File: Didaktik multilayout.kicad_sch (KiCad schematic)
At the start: 103 parts, among them J1 Conn_01x04_MountingPin, J2 AVR-ISP-6, SW1 SW_Push_45deg, SW10 SW_Push_45deg, SW11 SW_Push_45deg, SW12 SW_Push_45deg, SW13 SW_Push_45deg, SW14 SW_Push_45deg, SW15 SW_Push_45deg, SW16 SW_Push_45deg, SW17 SW_Push_45deg, SW18 SW_Push_45deg, SW19 SW_Push_45deg, SW2 SW_Push_45deg, SW20 SW_Push_45deg, SW21 SW_Push_45deg, SW22 SW_Push_45deg, SW23 SW_Push_45deg, SW24 SW_Push_45deg, SW25 SW_Push_45deg, SW26 SW_Push_45deg, SW27 SW_Push_45deg, SW28 SW_Push_45deg, SW29 SW_Push_45deg, SW3 SW_Push_45deg, SW30 SW_Push_45deg, SW31 SW_Push_45deg, SW32 SW_Push_45deg, SW33 SW_Push_45deg, SW34 SW_Push_45deg, SW35 SW_Push_45deg, SW36 SW_Push_45deg, SW37 SW_Push_45deg, SW38 SW_Push_45deg, SW39 SW_Push_45deg, SW4 SW_Push_45deg, SW40 SW_Push_45deg, SW5 SW_Push_45deg, SW6 SW_Push_45deg, SW7 SW_Push_45deg, SW8 SW_Push_45deg, SW9 SW_Push_45deg, U1 ATmega32U4-M, Y1 Crystal_GND24_Small

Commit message: routing multipcb
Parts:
- added SW31a1, SW32a1, SW33a1, SW34a1, SW37a1, SW38a1, SW39a1, SW40a1: SW_Push_45deg, Keebio-Parts:MX-Alps-Choc-1U-NoLED, symbol Switch:SW_Push_45deg
- added SW34b1, SW37b1: SW_Push_45deg, Keebio-Parts:MX-Alps-Choc-3U-NoLED-StabFlip, symbol Switch:SW_Push_45deg
- added SW35a1, SW36a1: SW_Push_45deg, Keebio-Parts:MX-Alps-Choc-1.5U-NoLED, symbol Switch:SW_Push_45deg
- added SW35b1, SW36b1: SW_Push_45deg, Keebio-Parts:MX-Alps-Choc-2U-NoLED-StabFlip, symbol Switch:SW_Push_45deg
- added SW35c1: SW_Push_45deg, Keebio-Parts:MX-Alps-Choc-6U-NoLED-StabFlip, symbol Switch:SW_Push_45deg
- added SW36c1: SW_Push_45deg, Keebio-Parts:MX-Alps-Choc-7U-NoLED-StabFlip, symbol Switch:SW_Push_45deg
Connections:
- net COL0: now also SW31a1.1, SW32a1.1
- net COL1: now also SW33a1.1, SW34a1.1, SW34b1.1
- net COL2: now also SW35a1.1, SW35b1.1, SW35c1.1, SW36a1.1, SW36b1.1, SW36c1.1
- net COL3: now also SW37a1.1, SW37b1.1, SW38a1.1
- net COL4: now also SW39a1.1, SW40a1.1
- net MISO: now also U1.20 (PD2); no longer U1.28 (PB4)
- net MOSI: now also U1.21 (PD3); no longer U1.26 (PD6)
- net ROW4: now also U1.30 (PB6); no longer U1.22 (PD5)
- net ROW5: now also U1.29 (PB5); no longer U1.21 (PD3)
- net ROW6: now also U1.28 (PB4); no longer U1.30 (PB6)
- net ROW7: now also U1.27 (PD7); no longer U1.29 (PB5)
- net SCK: now also U1.22 (PD5); no longer U1.27 (PD7)
- net at D37.2 (A), SW39.2: now also SW39a1.2
- net at D8.2 (A), SW32.2: now also SW32a1.2
- net at D33.2 (A), SW38.2: now also SW38a1.2
- net at D20.2 (A), SW35.2: now also SW35a1.2, SW35b1.2, SW35c1.2, SW36c1.2
- net at D41.2 (A), SW40.2: now also SW40a1.2
- net at D24.2 (A), SW36.2: now also SW36a1.2, SW36b1.2
- net at D12.2 (A), SW33.2: now also SW33a1.2
- net at D16.2 (A), SW34.2: now also SW34a1.2, SW34b1.2
- net at D29.2 (A), SW37.2: now also SW37a1.2, SW37b1.2
- net at D4.2 (A), SW31.2: now also SW31a1.2

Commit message: set up multilayout
need to check if all switches are really routed
maybe get rid of 2U
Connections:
- net MISO: now also U1.21 (PD3); no longer U1.20 (PD2)
- net MOSI: now also U1.22 (PD5); no longer U1.21 (PD3)
- net SCK: now also U1.20 (PD2); no longer U1.22 (PD5)
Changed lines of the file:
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@@
     )
   )
-  (global_label "MOSI" (shape input) (at 85.09 78.74 0) (fields_autoplaced)
+  (global_label "MOSI" (shape input) (at 85.09 83.82 0) (fields_autoplaced)
     (effects (font (size 1.27 1.27)) (justify left))
-    (property "Intersheet References" "${INTERSHEET_REFS}" (id 0) (at 92.0993 78.6606 0)
+    (property "Intersheet References" "${INTERSHEET_REFS}" (id 0) (at 92.0993 83.7406 0)
       (effects (font (size 1.27 1.27)) (justify left) hide)
     )
@@
     )
   )
-  (global_label "MISO" (shape input) (at 85.09 76.2 0) (fields_autoplaced)
+  (global_label "MISO" (shape input) (at 85.09 78.74 0) (fields_autoplaced)
     (effects (font (size 1.27 1.27)) (justify left))
-    (property "Intersheet References" "${INTERSHEET_REFS}" (id 0) (at 92.0993 76.1206 0)
+    (property "Intersheet References" "${INTERSHEET_REFS}" (id 0) (at 92.0993 78.6606 0)
       (effects (font (size 1.27 1.27)) (justify left) hide)
     )
@@
     )
   )
-  (global_label "SCK" (shape input) (at 85.09 83.82 0) (fields_autoplaced)
+  (global_label "SCK" (shape input) (at 85.09 76.2 0) (fields_autoplaced)
     (effects (font (size 1.27 1.27)) (justify left))
-    (property "Intersheet References" "${INTERSHEET_REFS}" (id 0) (at 91.2526 83.7406 0)
+    (property "Intersheet References" "${INTERSHEET_REFS}" (id 0) (at 91.2526 76.1206 0)
       (effects (font (size 1.27 1.27)) (justify left) hide)
     )

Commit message: changes
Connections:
- net GND: now also J1.MP (MountPin)
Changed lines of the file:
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@@
   (junction (at 37.465 146.05) (diameter 0) (color 0 0 0 0)
   )
+  (junction (at 69.215 185.42) (diameter 0) (color 0 0 0 0)
+  )
   (junction (at 189.23 69.85) (diameter 0) (color 0 0 0 0)
   )
@@
     (stroke (width 0) (type default) (color 0 0 0 0))
   )
+  (wire (pts (xy 74.295 190.5) (xy 69.215 190.5))
+    (stroke (width 0) (type default) (color 0 0 0 0))
+  )
   (wire (pts (xy 170.18 83.185) (xy 170.18 102.87))
     (stroke (width 0) (type default) (color 0 0 0 0))
@@
     (stroke (width 0) (type default) (color 0 0 0 0))
   )
+  (wire (pts (xy 69.215 190.5) (xy 69.215 185.42))
+    (stroke (width 0) (type default) (color 0 0 0 0))
+  )

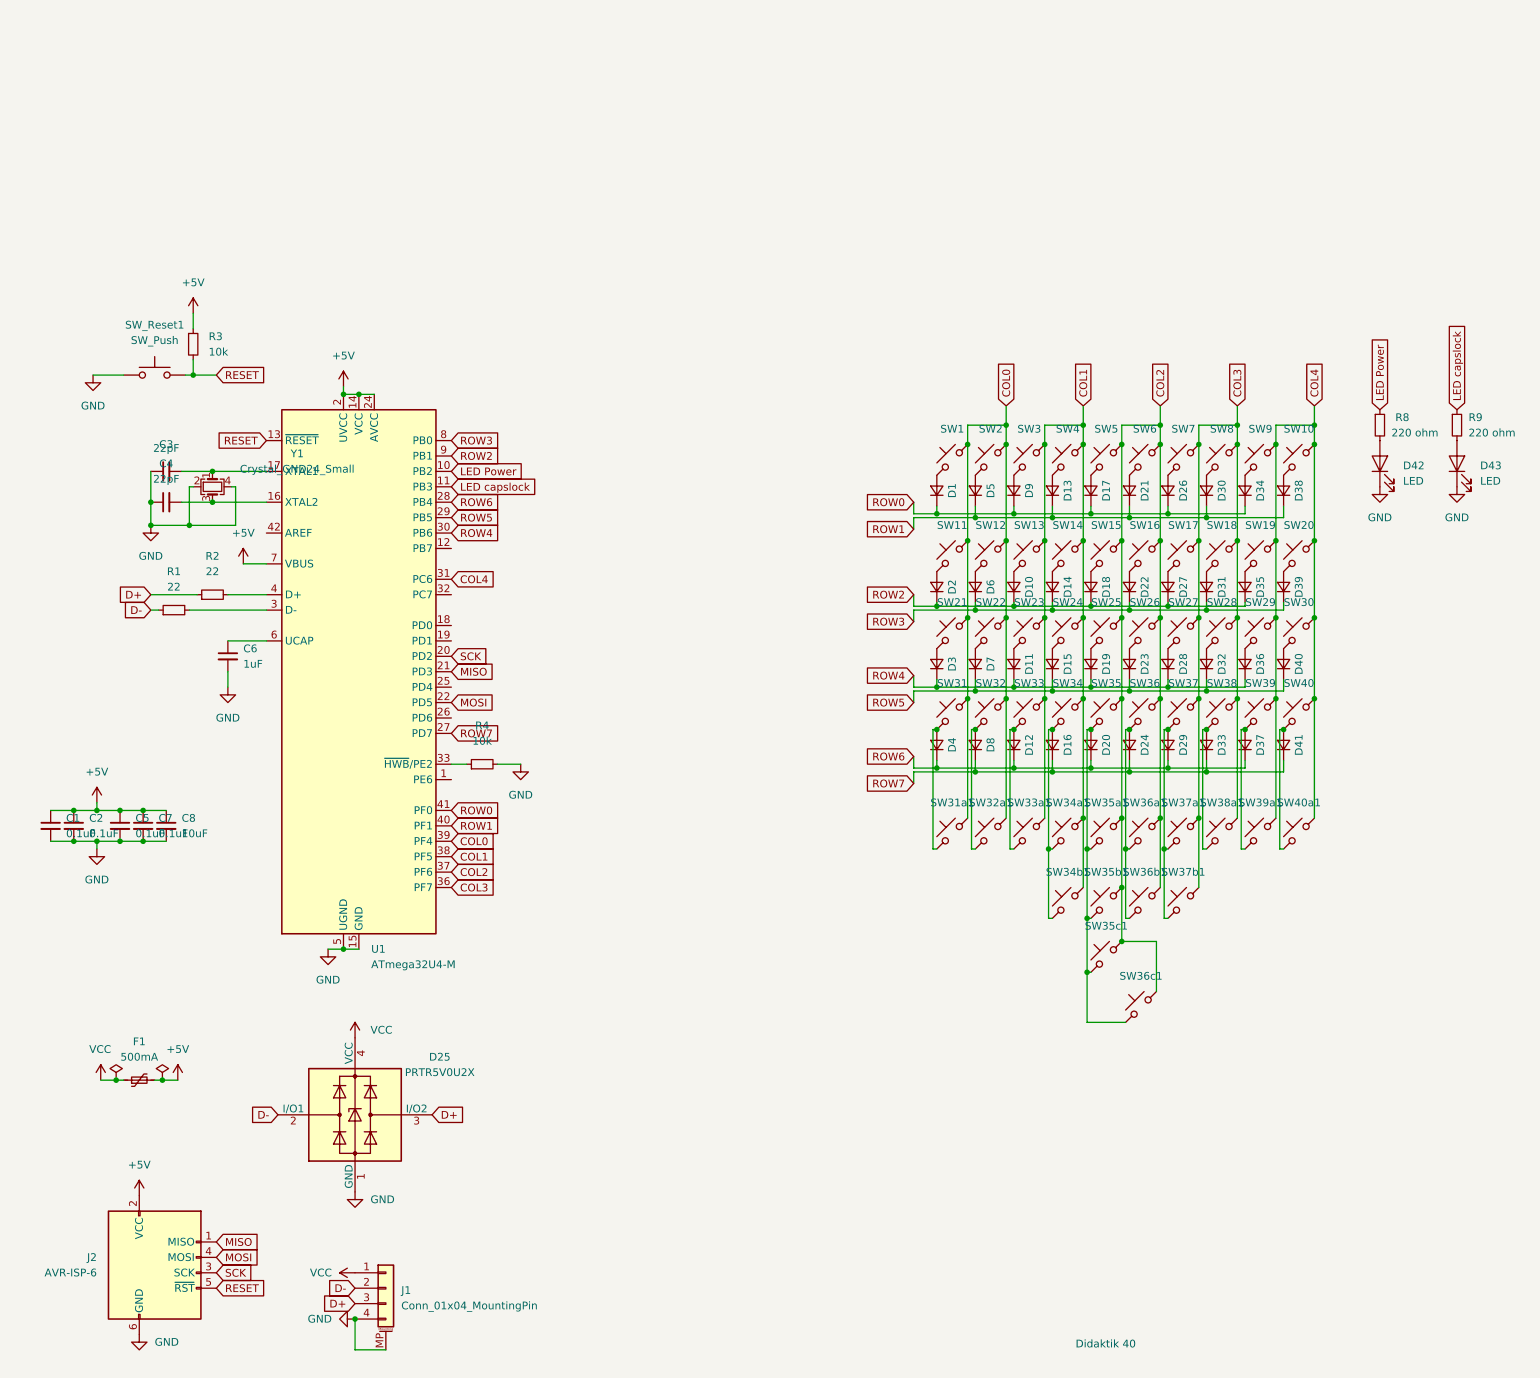
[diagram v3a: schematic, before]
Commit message: simplifying schematics, rerouting pcb
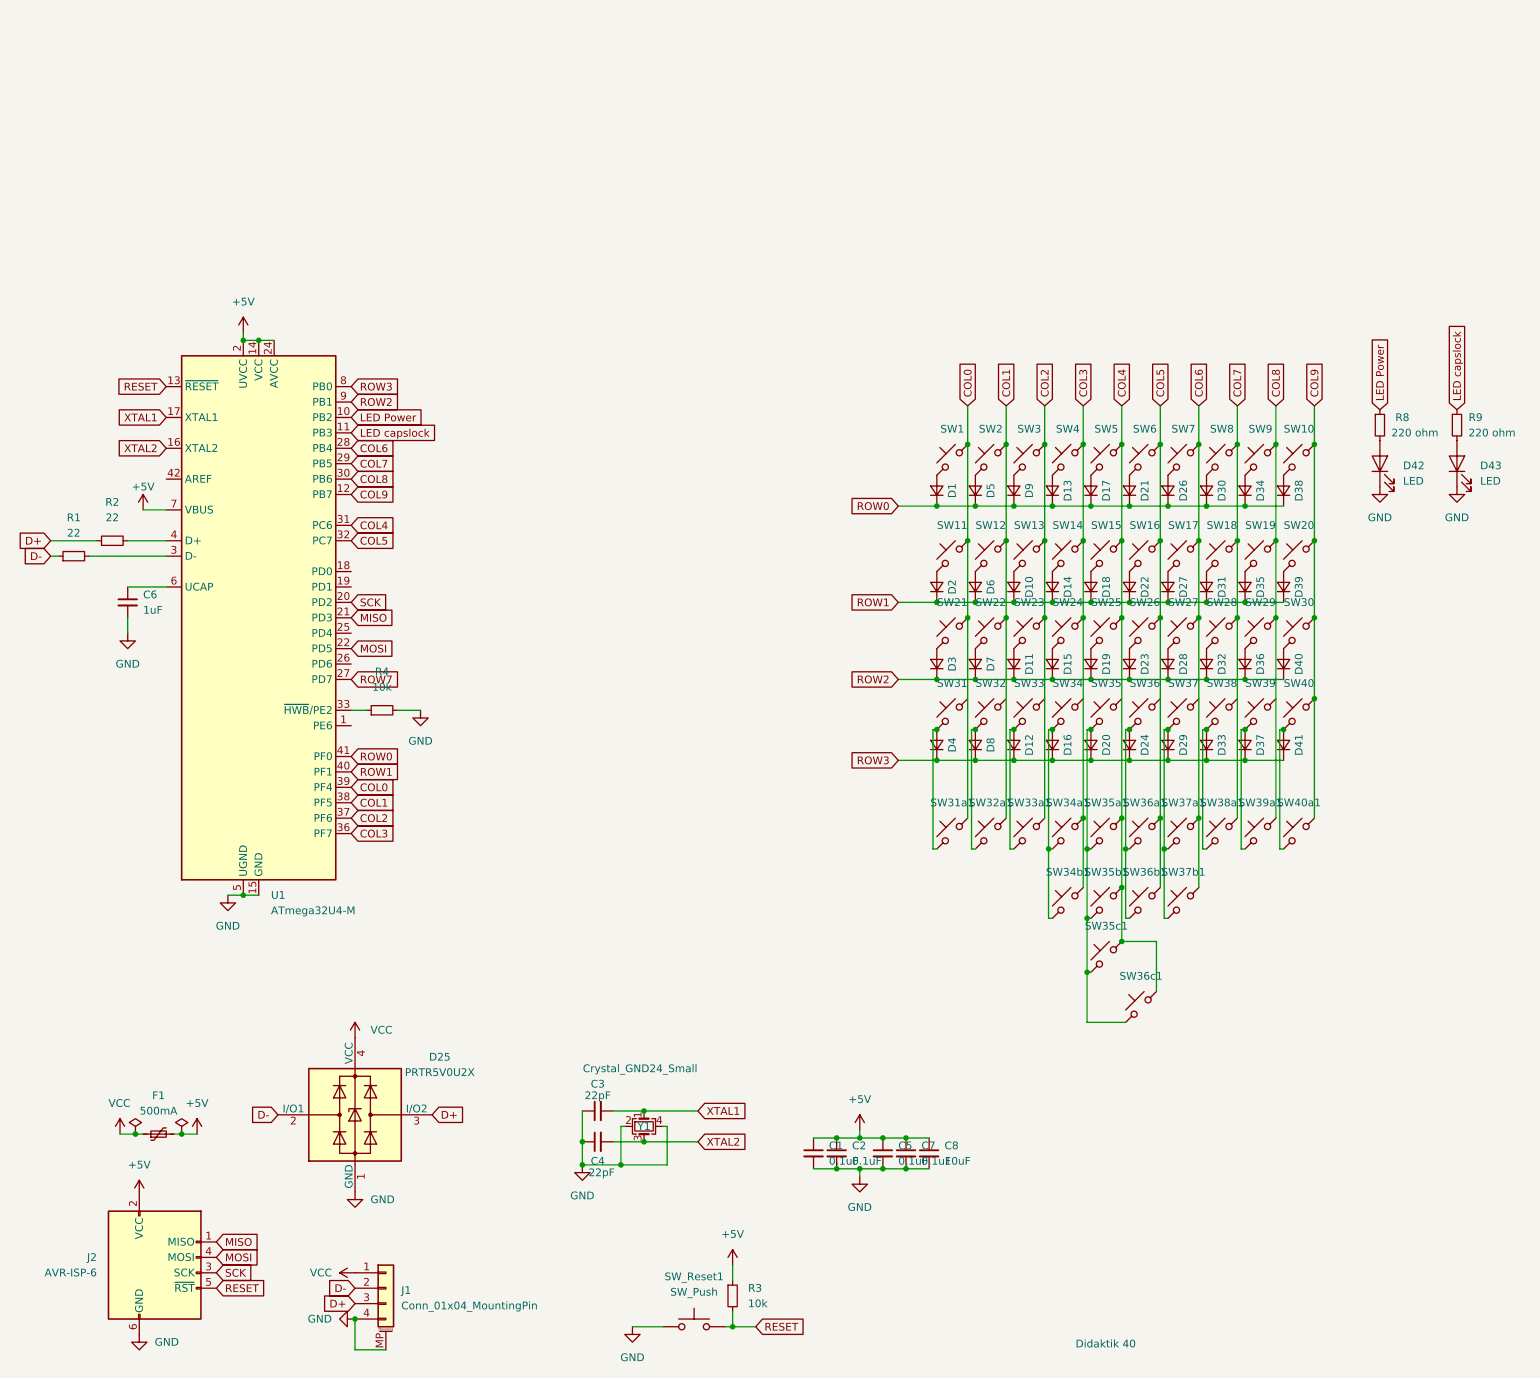
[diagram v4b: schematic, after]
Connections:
- net COL0: no longer SW12.1, SW2.1, SW22.1, SW31.1, SW32.1, SW32a1.1
- net COL1: now also SW12.1, SW2.1, SW22.1, SW32a1.1; no longer SW13.1, SW14.1, SW23.1, SW24.1, SW3.1, SW33.1, SW33a1.1, SW34.1, SW34a1.1, SW34b1.1, SW4.1
- net COL2: now also SW13.1, SW23.1, SW3.1, SW33a1.1; no longer SW15.1, SW16.1, SW25.1, SW26.1, SW35.1, SW35a1.1, SW35b1.1, SW35c1.1, SW36.1, SW36a1.1, SW36b1.1, SW36c1.1, SW5.1, SW6.1
- net COL3: now also SW14.1, SW24.1, SW34a1.1, SW34b1.1, SW4.1; no longer SW17.1, SW18.1, SW27.1, SW28.1, SW37.1, SW37a1.1, SW37b1.1, SW38.1, SW38a1.1, SW7.1, SW8.1
- net COL4: now also SW15.1, SW25.1, SW35a1.1, SW35b1.1, SW35c1.1, SW36c1.1, SW5.1; no longer SW10.1, SW19.1, SW20.1, SW29.1, SW30.1, SW39.1, SW39a1.1, SW40.1, SW40a1.1, SW9.1
- net ROW0: now also D13.1 (K), D21.1 (K), D30.1 (K), D38.1 (K), D5.1 (K)
- net ROW1: now also D10.1 (K), D14.1 (K), D18.1 (K), D2.1 (K), D22.1 (K), D27.1 (K), D31.1 (K), D35.1 (K), D39.1 (K), D6.1 (K); no longer D13.1 (K), D21.1 (K), D30.1 (K), D38.1 (K), D5.1 (K)
- net ROW2: now also D11.1 (K), D15.1 (K), D19.1 (K), D23.1 (K), D28.1 (K), D3.1 (K), D32.1 (K), D36.1 (K), D40.1 (K), D7.1 (K); no longer D10.1 (K), D18.1 (K), D2.1 (K), D27.1 (K), D35.1 (K)
- net ROW3: now also D12.1 (K), D16.1 (K), D20.1 (K), D24.1 (K), D29.1 (K), D33.1 (K), D37.1 (K), D4.1 (K), D41.1 (K), D8.1 (K); no longer D14.1 (K), D22.1 (K), D31.1 (K), D39.1 (K), D6.1 (K)
- net ROW7: no longer D16.1 (K), D24.1 (K), D33.1 (K), D41.1 (K), D8.1 (K)
- net XTAL1: now reaches C3.2, U1.17 (XTAL1), Y1.1
- net XTAL2: now reaches C4.2, U1.16 (XTAL2), Y1.3
- net COL9: now reaches U1.12 (PB7)
- net COL9: now also SW10.1, SW20.1, SW30.1, SW40.1, SW40a1.1
- net COL5: now reaches U1.32 (PC7)
- net COL5: now also SW16.1, SW26.1, SW36a1.1, SW36b1.1, SW6.1
- removed net ROW4: D11.1 (K), D19.1 (K), D28.1 (K), D3.1 (K), D36.1 (K), U1.30 (PB6)
- removed net ROW5: D15.1 (K), D23.1 (K), D32.1 (K), D40.1 (K), D7.1 (K), U1.29 (PB5)
- removed net ROW6: D12.1 (K), D20.1 (K), D29.1 (K), D37.1 (K), D4.1 (K), U1.28 (PB4)
- new net COL6: SW17.1, SW27.1, SW37a1.1, SW37b1.1, SW7.1, U1.28 (PB4)
- new net COL7: SW18.1, SW28.1, SW38a1.1, SW8.1, U1.29 (PB5)
- new net COL8: SW19.1, SW29.1, SW39a1.1, SW9.1, U1.30 (PB6)
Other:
- moved on the sheet: C1, C2, C3, C4, C5, C6, C7, C8, F1, R1, R2, R3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
